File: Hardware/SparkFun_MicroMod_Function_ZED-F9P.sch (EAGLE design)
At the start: 98 parts, among them J2 MICROMOD_STANDARD, J3 QWIIC_RA, J4 U.FL, Q1 DMP21D0UT, Q2 600mA/40V, Q3 600mA/40V, U1 EEPROM, U2 U-BLOX_ZED-F9P, U4 SN74AUP1T04DCK, U5 PCA9306DCUR, U6 74LVC541ABQ, U7 MIC5219 3.3V, U8 MIC5219 3.3V, U9 74LVC541ABQ

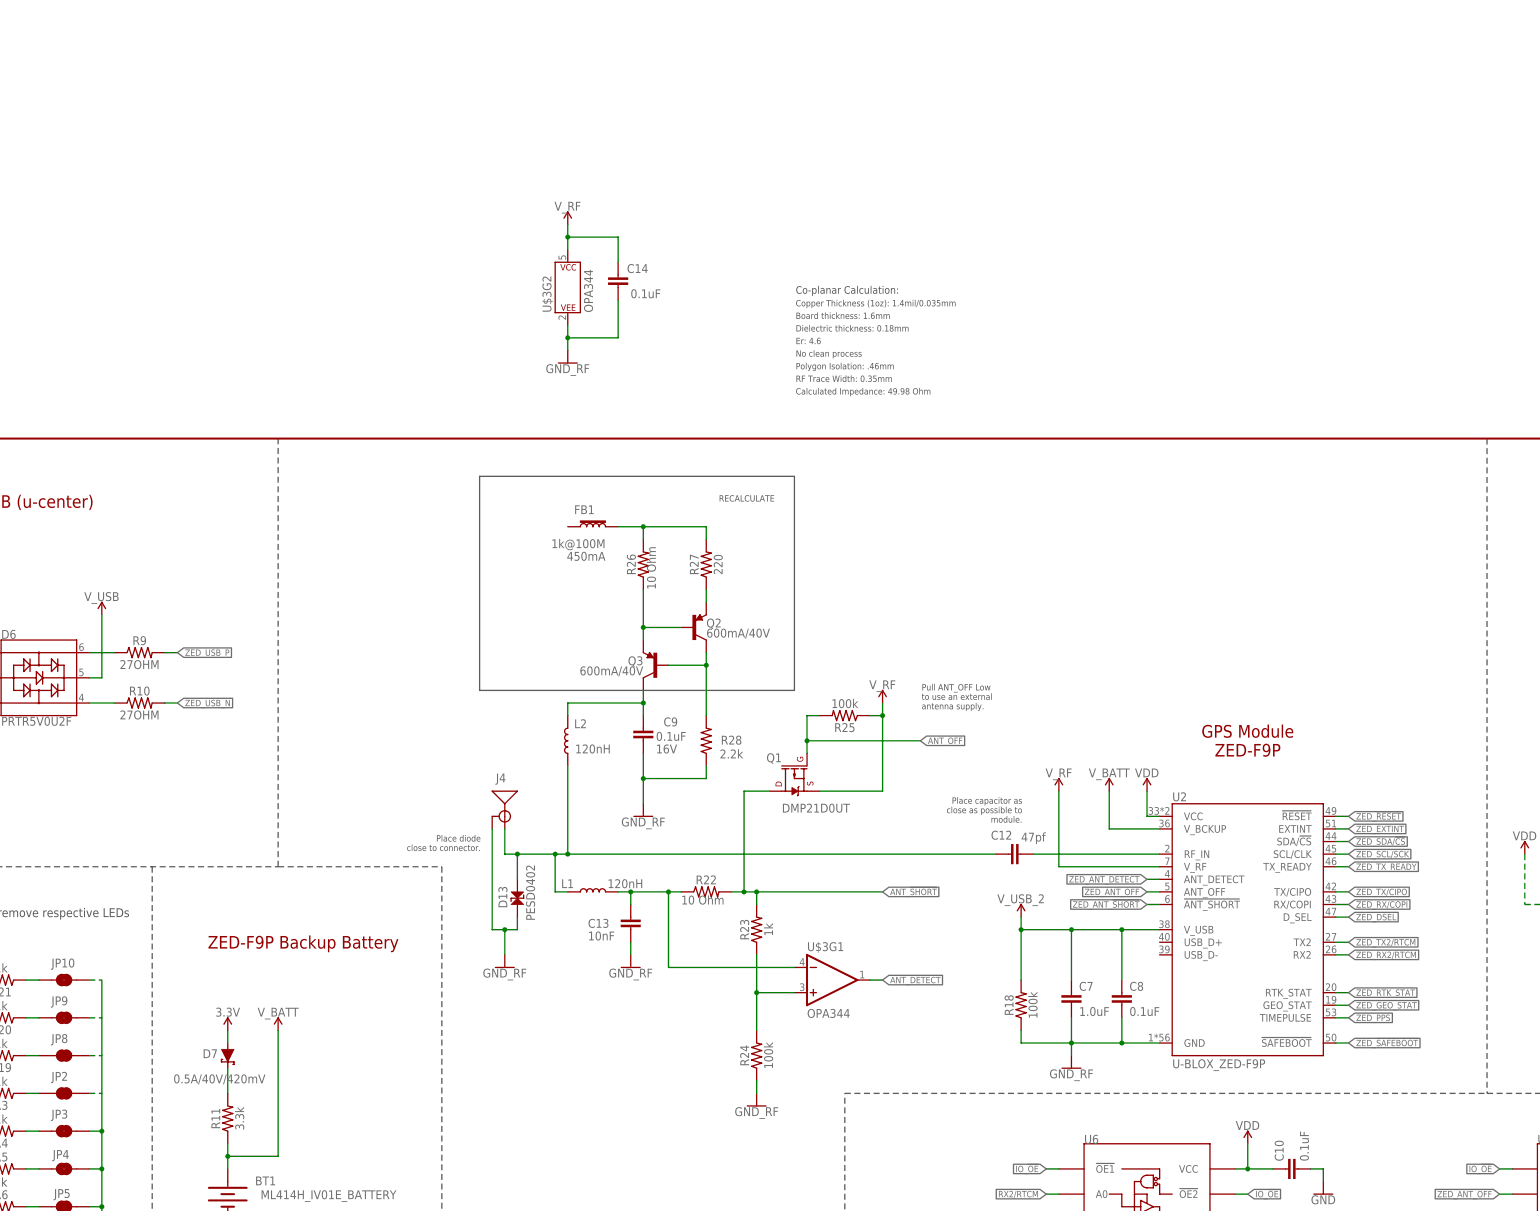
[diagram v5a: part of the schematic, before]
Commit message: Commit for current progress.
Committing so others can begin a schematic review while I finish up.
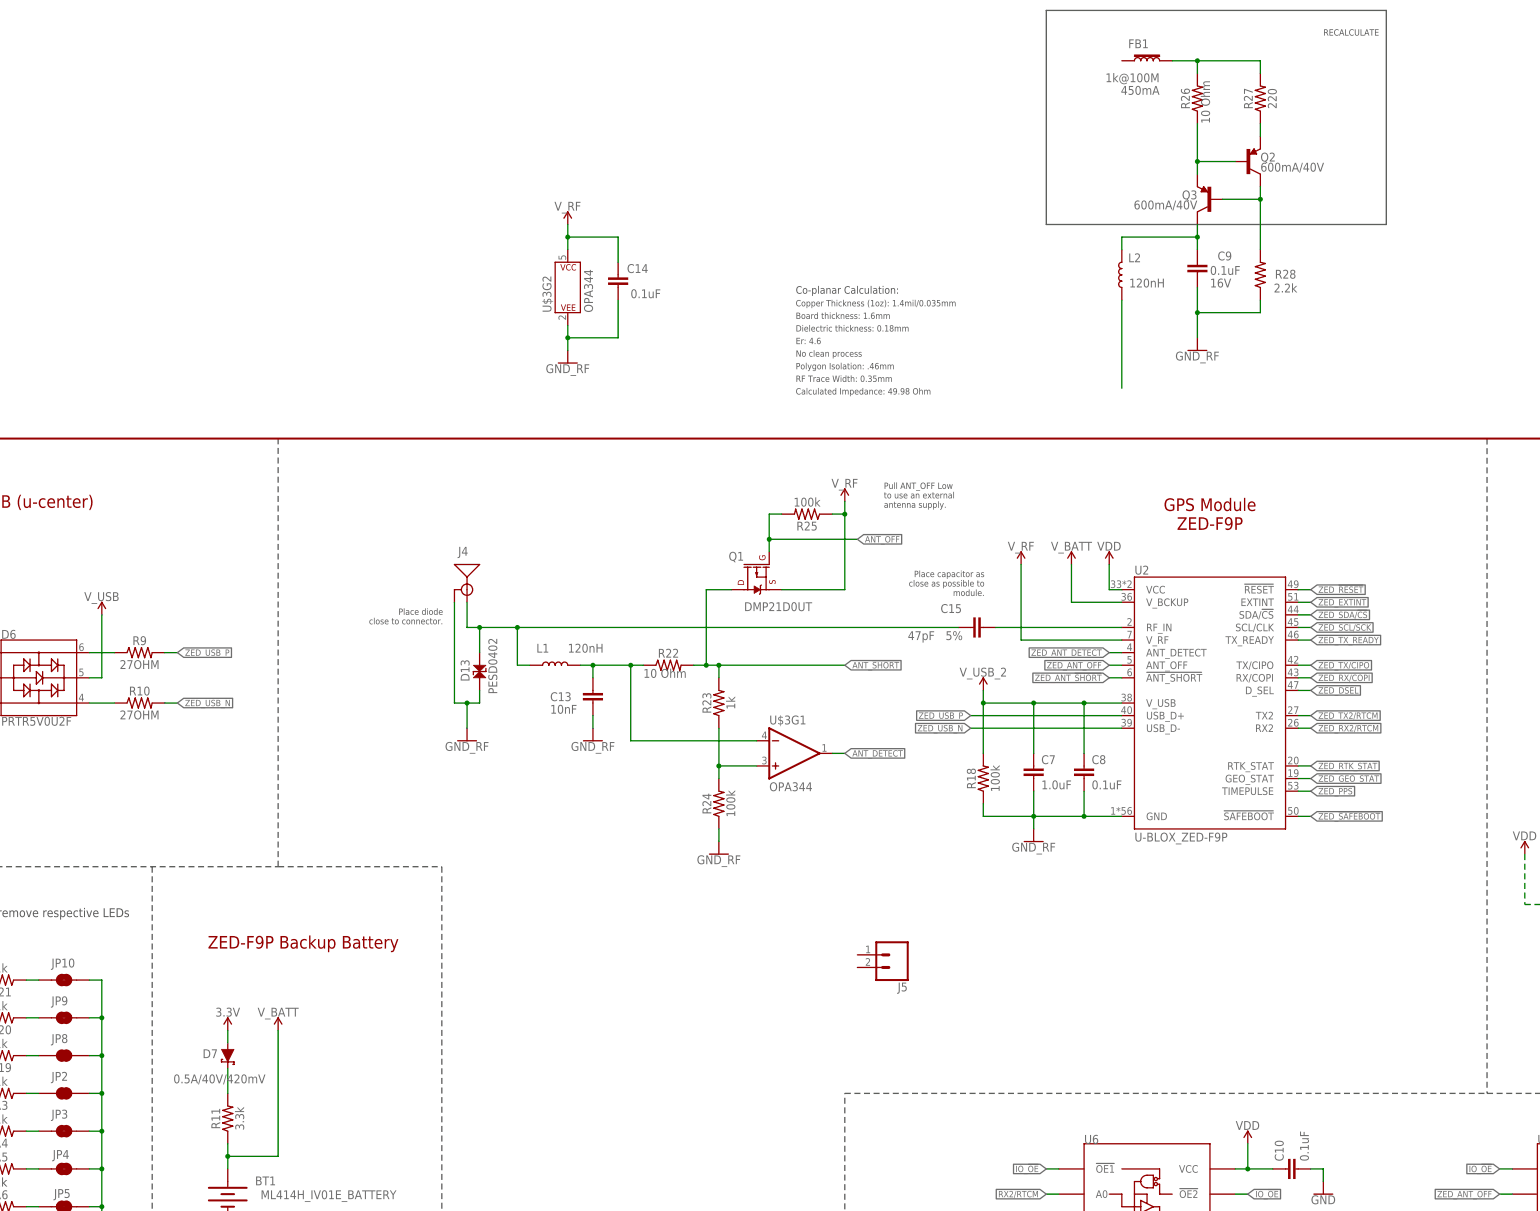
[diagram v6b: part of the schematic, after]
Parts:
- removed C12: GRM0335C1H470JA01, MicroMod_Function_GNSS_ublox_ZED_F9P:GRM0335C1H470JA01
- added C15: CBR04C470J5GAC, MicroMod_Function_GNSS_ublox_ZED_F9P:CBR04C470J5GAC
- added J5: (no value), SparkFun-Connectors:CONN_02PTH4
- L1: value LQW15ANR12J00D -> LQW18ANR12J8ZD; device MicroMod_Function_GNSS_ublox_ZED_F9P:LQW15ANR12J00D -> MicroMod_Function_GNSS_ublox_ZED_F9P:LQW18ANR12J8ZD; INDUCTANCE 120nH -> (none)
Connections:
- new net SMA_RF_IN1: L2.1
- net RF_IN: now also C15.2; no longer C12.2
- net SMA_RF_IN: now also C15.1; no longer C12.1, L2.1
- net ZED_USB_N: now also U2.USB_D-
- net ZED_USB_P: now also U2.USB_D+
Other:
- moved on the sheet: C13, C7, C8, C9, D13, FB1, J4, L1, L2, Q1, Q2, Q3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

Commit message: Schematic V1.0
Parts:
- removed FB1: BLM18AG102BH1D, MicroMod_Function_GNSS_ublox_ZED_F9P:BLM18AG102BH1D
- removed L2: LQW15ANR12J00D, MicroMod_Function_GNSS_ublox_ZED_F9P:LQW15ANR12J00D
- removed Q2, Q3: 600mA/40V, SparkFun-DiscreteSemi:TRANS_PNP-MMBT4403
- removed R27: 220, SparkFun-Resistors:220OHM-0603-1/10W-1%
- removed R28: 2.2k, SparkFun-Resistors:2.2KOHM-0603-1/10W-1%
- added C12: 0.1uF, SparkFun-Capacitors:0.1UF-0402-16V-10%
- added C16, C17: 0.1uF, SparkFun-Capacitors:0.1UF-0603-25V-(+80/-20%)
- added J6, J7: (no value), SparkFun-Connectors:CONN_01
- added SUPPLY35: 2PT_GND_TIE, SparkFun-PowerSymbols:2PT_GND_TIE
- added TP1, TP10, TP11, TP12, TP13, TP14, TP15, TP16, TP17, TP18, TP19, TP2, TP20, TP3, TP4, TP5, TP6, TP8: TEST-POINT3, SparkFun-Connectors:TEST-POINT3
- added TP7, TP9: TEST-POINTPOGO_PTH, SparkFun-Connectors:TEST-POINTPOGO_PTH
- added U$7: OPA344, SparkFun-IC-Amplifiers:OPA344
- added U3: FIN1017MXSOIC-8, MicroMod_Function_GNSS_ublox_ZED_F9P:FIN1017MXSOIC-8
- C9: value 0402YD104JAT2A -> 1.0uF; device MicroMod_Function_GNSS_ublox_ZED_F9P:0402YD104JAT2A -> SparkFun-Capacitors:1.0UF-0603-16V-10%; CAPACITANCE 0.1uF -> (none); VOLTAGE 16V -> (none)
- J5: device SparkFun-Connectors:CONN_02PTH4 -> SparkFun-Connectors:CONN_02-JST-2MM-SMT
- L1: value LQW18ANR12J8ZD -> LQW15AWR15J80D; device MicroMod_Function_GNSS_ublox_ZED_F9P:LQW18ANR12J8ZD -> MicroMod_Function_GNSS_ublox_ZED_F9P:LQW15AWR15J80D
- R22: value CRGP2010F10R -> 20; device MicroMod_Function_GNSS_ublox_ZED_F9P:CRGP2010F10R -> SparkFun-Resistors:20OHM-0603-1/10W-1%; RESISTANCE 10 Ohm -> (none)
- R23: value 1k -> 2.0k; device SparkFun-Resistors:1KOHM-0603-1/10W-1% -> SparkFun-Resistors:2.0KOHM-0603-1/10W-5%
- R25: value 100k -> 10k; device SparkFun-Resistors:100KOHM-0603-1/10W-1% -> SparkFun-Resistors:10KOHM-0603-1/10W-1%
- R26: value CRGP2010F10R -> DNP; device MicroMod_Function_GNSS_ublox_ZED_F9P:CRGP2010F10R -> SparkFun-Resistors:DNP-0603_NO_CREAM; RESISTANCE 10 Ohm -> (none)
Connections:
- removed net N$21: J2.F2/PWM
- removed net N$22: J2.F3
- removed net N$23: J2.F4
- removed net N$25: J2.F5
- removed net N$52: Q2.E, R27.1
- removed net N$53: FB1.2, R26.2, R27.2
- removed net SMA_RF_IN: C15.1, D13.2, J4.SIGNAL, L1.1
- removed net SMA_RF_IN1: L2.1
- net !RESET!: now also J2.F3, TP14.1
- net !SAFEBOOT!: now also J2.F5, TP12.1
- net 3.3V: now also C16.1, TP8.1
- net ANT_!SHORT!: now also R22.1; no longer R22.2
- net ANT_DETECT: now also U$7G1.OUT; no longer U$3G1.OUT
- net ANT_OFF: now also R26.1
- net EXTINT: now also J2.F4; no longer J2.I2C_!INT!
- net GND: now also C12.2, C16.2, C17.1, C3.2, C5.2, SUPPLY35.P$2, TP1.1, TP2.1, TP7.1, U3.GND
- net GND_RF: now also D13.2, R25.1, SUPPLY35.P$1, TP4.1, TP9.1; no longer C3.2, C5.2, D13.1, R28.1
- net N$41: now also C15.1, D13.1, J4.SIGNAL, L1.2; no longer C9.1, L2.2, Q3.C
- net N$48: now also U$7G1.+IN; no longer U$3G1.+IN
- net N$49: now also L1.1, R22.2, U$7G1.-IN; no longer L1.2, R22.1, U$3G1.-IN
- net N$50: now also J5.2, U3.DO+; no longer Q2.B, Q3.E, R26.1
- net N$51: now also J5.1, U3.DO-; no longer Q2.C, Q3.B, R28.2
- net PPS: now also J2.F2/PWM, TP13.1, U3.DIN
- net RX/COPI: now also TP15.1
- net RX2/RTCM: now also J6.1, TP17.1
- net SCL/SCK: now also TP19.1
- net SDA/!CS!: now also TP20.1
- net TX/CIPO: now also TP16.1
- net TX2/RTCM: now also J7.1, TP18.1
- net VCC: now also C12.1, TP6.1, U3.VCC
- net VDD: now also C14.2, C17.2, C9.1, TP3.1, U$3G2.P$V+
- net V_BATT: now also TP5.1
- net V_RF: now also R26.2; no longer C14.2, R25.1, U$3G2.P$V+
- net V_USB: now also TP10.1
- net V_USB_2: now also TP11.1
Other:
- note added: "Board thickness: 0.8mm"
- note added: "External Breakout"
- note added: "I/O Decoupling Control"
- note added: "Pull ANT_OFF High to use antenna supervisor."
- note added: "RF/ANTENNA SUPERVISION"
- note removed: "Board thickness: 1.6mm"
- note removed: "Decoupling Control"
- note removed: "Pull ANT_OFF Low to use an external antenna supply."
- note removed: "RECALCULATE"
- moved on the sheet: BT1, C1, C10, C11, C13, C14, C15, C3, C4, C6, C7, C8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

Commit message: Added  Correct Version to sch.
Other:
- note added: "v1.0"
- note removed: "v0.1"
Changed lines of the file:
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@@
 <text x="119.634" y="91.186" size="2.54" layer="94" font="vector" align="center">MicroMod Function Connector</text>
 <text x="348.234" y="11.176" size="2.54" layer="94">A. Brudner</text>
-<text x="421.894" y="6.096" size="2.54" layer="94">v0.1</text>
+<text x="421.894" y="6.096" size="2.54" layer="94">v1.0</text>
 <wire x1="160.02" y1="66.04" x2="160.02" y2="0" width="0.2032" layer="97" style="longdash"/>
 <wire x1="0" y1="106.68" x2="83.82" y2="106.68" width="0.2032" layer="97" style="longdash"/>
